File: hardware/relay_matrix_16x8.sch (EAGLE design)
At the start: 275 parts, among them J6 CT3151, J7 CT3151, J8 CT3151, U1 TM4C123GH6PMI, U2 CP2102N-A02-GQFN24R, U20 SN74HCS595, U21 SN74HCS595, U22 SN74HCS595, U23 SN74HCS595, U30 LDD-SMHTA304RISITR, U31 LDD-SMHTA304RISITR, U32 LDD-SMHTA304RISITR, U33 LDD-SMHTA304RISITR, U34 LDD-SMHTA304RISITR, U35 LDD-SMHTA304RISITR, U36 LDD-SMHTA304RISITR, U37 LDD-SMHTA304RISITR, U38 LDD-SMHTA304RISITR, U4 TLS835B2ELVSE, U5 TLS835B2ELVSE, X1 2171790001, X101 364A2595, X102 364A2595, X103 364A2595, X104 364A2595, X105 364A2595, X106 364A2595, X107 364A2595, X108 364A2595, X111 364A2595, X112 364A2595, X113 364A2595, X114 364A2595, X2 FTSH-105-01-F-DV-007-K-P, X3 SJ1-3523NG, X4 SJ1-3523NG, X5 SJ1-3523NG

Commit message: replace LDOs with more common part
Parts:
- removed U5: TLS835B2ELVSE, TLS835B2ELVSEXUMA1:TLS835B2ELVSEXUMA1
- added R33, R35: 220, rcl:R-US_R0603
- added R34: 360, rcl:R-US_R0603
- added R36: 680, rcl:R-US_R0603
- added R37, R38: 1, rcl:R-US_R0603
- added U3: NCP1117XXA, 1117:NCP1117XXA
- C10, C7: value .1uF -> 10uF; device resistor:C-USC0402 -> rcl:C-USC0805
- C11, C12: value 1uF -> 10uF; device resistor:C-USC0402 -> rcl:C-USC0805
- C8, C9: value .1uF -> 1uF
- U4: value TLS835B2ELVSE -> NCP1117XXA; device TLS835B2ELVSEXUMA1:TLS835B2ELVSEXUMA1 -> 1117:NCP1117XXA
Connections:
- net NRESET renamed !RST
- removed net 5V0: C12.1, C18.1, C31.1, C32.1, C33.1, C34.1, C35.1, C36.1, C37.1, C38.1, C39.1, C40.1, C41.1, C42.1, C43.1, C44.1, C45.1, C46.1, U100.LOADSUPPLY, U101.LOADSUPPLY, U102.LOADSUPPLY, U103.LOADSUPPLY, U104.LOADSUPPLY, U105.LOADSUPPLY, U106.LOADSUPPLY, U107.LOADSUPPLY, U108.LOADSUPPLY, U109.LOADSUPPLY, U110.LOADSUPPLY, U111.LOADSUPPLY, U112.LOADSUPPLY, U113.LOADSUPPLY, U114.LOADSUPPLY, U115.LOADSUPPLY, U5.Q, U5.SEL, U6.VCC
- removed net VDD: C1.1, C101.1, C102.1, C103.1, C104.1, C105.1, C106.1, C107.1, C108.1, C109.1, C110.1, C14.1, C15.1, C16.1, C17.1, C19.1, C2.1, C20.1, C21.1, C22.1, C23.1, C24.1, C25.1, C26.1, C27.1, C28.1, C29.1, C3.1, C30.1, C4.1, C5.1, C6.1, D1.HIGH, D2.HIGH, R14.2, R9.1, U1.VDD, U1.VDDA, U1.VDDC, U1.VDDC_2, U1.VDD_2, U1.VDD_3, U1.VDD_4, U100.LOGICSUPPLY, U101.LOGICSUPPLY, U102.LOGICSUPPLY, U103.LOGICSUPPLY, U104.LOGICSUPPLY, U105.LOGICSUPPLY, U106.LOGICSUPPLY, U107.LOGICSUPPLY, U108.LOGICSUPPLY, U109.LOGICSUPPLY, U110.LOGICSUPPLY, U111.LOGICSUPPLY, U112.LOGICSUPPLY, U113.LOGICSUPPLY, U114.LOGICSUPPLY, U115.LOGICSUPPLY, U2.VDD, U2.VIO, U2.VREGIN, U20.VCC, U21.VCC, U22.VCC, U23.VCC, X2.VCC
- new net +5V: C18.1, C31.1, C32.1, C33.1, C34.1, C35.1, C36.1, C37.1, C38.1, C39.1, C40.1, C41.1, C42.1, C43.1, C44.1, C45.1, R35.2, R38.2, U100.LOADSUPPLY, U101.LOADSUPPLY, U102.LOADSUPPLY, U103.LOADSUPPLY, U104.LOADSUPPLY, U105.LOADSUPPLY, U106.LOADSUPPLY, U107.LOADSUPPLY, U108.LOADSUPPLY, U109.LOADSUPPLY, U110.LOADSUPPLY, U111.LOADSUPPLY, U112.LOADSUPPLY, U113.LOADSUPPLY, U114.LOADSUPPLY, U115.LOADSUPPLY, U3.VOUT
- new net N$20: C9.1, R33.1, R34.2, U4.ADJ/GND
- new net N$21: C8.1, R35.1, R36.2, U3.ADJ/GND
- new net N$22: C11.1, R37.1
- new net N$23: C12.1, R38.1
- new net VDDC: C107.1, C108.1, C109.1, C110.1, U1.VDDC, U1.VDDC_2
- net +12V: now also U3.VIN, U4.VIN; no longer C8.1, C9.1, U4.EN, U4.I, U5.EN, U5.I
- net GND: now also R34.1, R36.1, S2.P$3, S2.P$4, X2.GDTCT; no longer S2.P$1, S2.P$2, U4.GND, U4.SEL, U5.GND
- net N$19: now also S2.P$1, S2.P$2; no longer S2.P$3, S2.P$4
- net VBUS: now also C46.1, U6.VCC; no longer U6.IO3
- net VCC: now also C1.1, C101.1, C102.1, C103.1, C104.1, C105.1, C106.1, C14.1, C15.1, C16.1, C17.1, C19.1, C2.1, C20.1, C21.1, C22.1, C23.1, C24.1, C25.1, C26.1, C27.1, C28.1, C29.1, C3.1, C30.1, C4.1, C5.1, C6.1, D1.HIGH, D2.HIGH, R14.2, R33.2, R37.2, R9.1, U1.VDD, U1.VDDA, U1.VDD_2, U1.VDD_3, U1.VDD_4, U100.LOGICSUPPLY, U101.LOGICSUPPLY, U102.LOGICSUPPLY, U103.LOGICSUPPLY, U104.LOGICSUPPLY, U105.LOGICSUPPLY, U106.LOGICSUPPLY, U107.LOGICSUPPLY, U108.LOGICSUPPLY, U109.LOGICSUPPLY, U110.LOGICSUPPLY, U111.LOGICSUPPLY, U112.LOGICSUPPLY, U113.LOGICSUPPLY, U114.LOGICSUPPLY, U115.LOGICSUPPLY, U2.VDD, U2.VIO, U2.VREGIN, U20.VCC, U21.VCC, U22.VCC, U23.VCC, U4.VOUT, X2.VCC; no longer C11.1, U4.Q
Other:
- note added: "Microcontroller"
- note added: "Power connectors"
- note added: "UART connectors"
- note added: "Voltage regulators"

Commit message: version sent to pcbway
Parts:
- added C47: 100n, resistor:C-USC0402
- added U5: ECS-2033-080-AU, ecs-20xx:ECS-2033-080-AU
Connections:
- new net OSC: U1.XOSC0, U5.OSC
- net GND: now also C47.2, U5.GND
- net VCC: now also C47.1, U5.EN, U5.VDD
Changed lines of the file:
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@@
 <part name="R37" library="rcl" library_urn="urn:adsk.eagle:library:334" deviceset="R-US_" device="R0603" package3d_urn="urn:adsk.eagle:package:23555/3" value="1"/>
 <part name="R38" library="rcl" library_urn="urn:adsk.eagle:library:334" deviceset="R-US_" device="R0603" package3d_urn="urn:adsk.eagle:package:23555/3" value="1"/>
+<part name="U5" library="ecs-20xx" deviceset="ECS-2033-080-AU" device="" package3d_urn="urn:adsk.eagle:package:34367365/1"/>
+<part name="P+2" library="supply1" library_urn="urn:adsk.eagle:library:371" deviceset="VCC" device=""/>
+<part name="GND2" library="supply1" library_urn="urn:adsk.eagle:library:371" deviceset="GND" device=""/>
+<part name="C47" library="resistor" library_urn="urn:adsk.eagle:library:348" deviceset="C-US" device="C0402" package3d_urn="urn:adsk.eagle:package:23626/2" value="100n"/>
+<part name="GND28" library="supply1" library_urn="urn:adsk.eagle:library:371" deviceset="GND" device=""/>
 </parts>
 <sheets>
@@
 <instance part="GND22" gate="1" x="20.32" y="-20.32" smashed="yes">
 <attribute name="VALUE" x="17.78" y="-22.86" size="1.778" layer="96"/>
+</instance>
+<instance part="U5" gate="G$1" x="144.78" y="-53.34" smashed="yes"/>
+<instance part="P+2" gate="VCC" x="137.16" y="-50.8" smashed="yes">
+<attribute name="VALUE" x="134.62" y="-53.34" size="1.778" layer="96" rot="R90"/>
+</instance>
+<instance part="GND2" gate="1" x="137.16" y="-78.74" smashed="yes">
+<attribute name="VALUE" x="134.62" y="-81.28" size="1.778" layer="96"/>
+</instance>
+<instance part="C47" gate="G$1" x="132.08" y="-63.5" smashed="yes">
+<attribute name="NAME" x="133.096" y="-62.865" size="1.778" layer="95"/>
+<attribute name="VALUE" x="133.096" y="-67.691" size="1.778" layer="96"/>
+</instance>
+<instance part="GND28" gate="1" x="132.08" y="-72.39" smashed="yes">
+<attribute name="VALUE" x="129.54" y="-74.93" size="1.778" layer="96"/>
 </instance>
 </instances>
@@
 <pinref part="GND12" gate="1" pin="GND"/>
 </segment>
+<segment>
+<pinref part="GND2" gate="1" pin="GND"/>
+<wire x1="137.16" y1="-76.2" x2="137.16" y2="-73.66" width="0.1524" layer="91"/>
+<pinref part="U5" gate="G$1" pin="GND"/>
+<wire x1="137.16" y1="-73.66" x2="139.7" y2="-73.66" width="0.1524" layer="91"/>
+</segment>
+<segment>
+<pinref part="C47" gate="G$1" pin="2"/>
+<pinref part="GND28" gate="1" pin="GND"/>
+<wire x1="132.08" y1="-69.85" x2="132.08" y2="-68.58" width="0.1524" layer="91"/>
+</segment>
 </net>
 <net name="MCU_RX_PAR" class="0">
@@
 <pinref part="P+14" gate="VCC" pin="VCC"/>
 </segment>
+<segment>
+<pinref part="P+2" gate="VCC" pin="VCC"/>
+<wire x1="137.16" y1="-53.34" x2="137.16" y2="-55.88" width="0.1524" layer="91"/>
+<pinref part="U5" gate="G$1" pin="EN"/>
+<wire x1="137.16" y1="-55.88" x2="137.16" y2="-58.42" width="0.1524" layer="91"/>
+<wire x1="137.16" y1="-58.42" x2="137.16" y2="-60.96" width="0.1524" layer="91"/>
+<wire x1="137.16" y1="-60.96" x2="139.7" y2="-60.96" width="0.1524" layer="91"/>
+<pinref part="U5" gate="G$1" pin="VDD"/>
+<wire x1="139.7" y1="-55.88" x2="137.16" y2="-55.88" width="0.1524" layer="91"/>
+<junction x="137.16" y="-55.88"/>
+<wire x1="137.16" y1="-58.42" x2="132.08" y2="-58.42" width="0.1524" layer="91"/>
+<wire x1="132.08" y1="-58.42" x2="132.08" y2="-60.96" width="0.1524" layer="91"/>
+<pinref part="C47" gate="G$1" pin="1"/>
+<junction x="137.16" y="-58.42"/>
+</segment>
 </net>
 <net name="!RST" class="0">
@@
 </segment>
 </net>
+<net name="OSC" class="0">
+<segment>
+<pinref part="U5" gate="G$1" pin="OSC"/>
+<wire x1="167.64" y1="-55.88" x2="172.72" y2="-55.88" width="0.1524" layer="91"/>
+<label x="172.72" y="-55.88" size="1.27" layer="95" xref="yes"/>
+</segment>
+<segment>
+<pinref part="U1" gate="A" pin="XOSC0"/>
+<wire x1="91.44" y1="16.51" x2="96.52" y2="16.51" width="0.1524" layer="91"/>
+<label x="96.52" y="16.51" size="1.27" layer="95" xref="yes"/>
+</segment>
+</net>

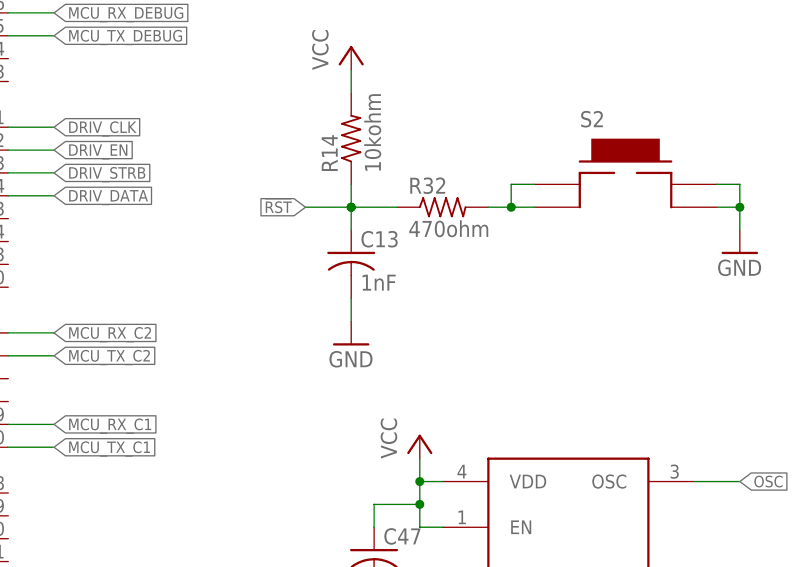
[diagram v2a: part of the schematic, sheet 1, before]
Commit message: finish filling out part ordering info
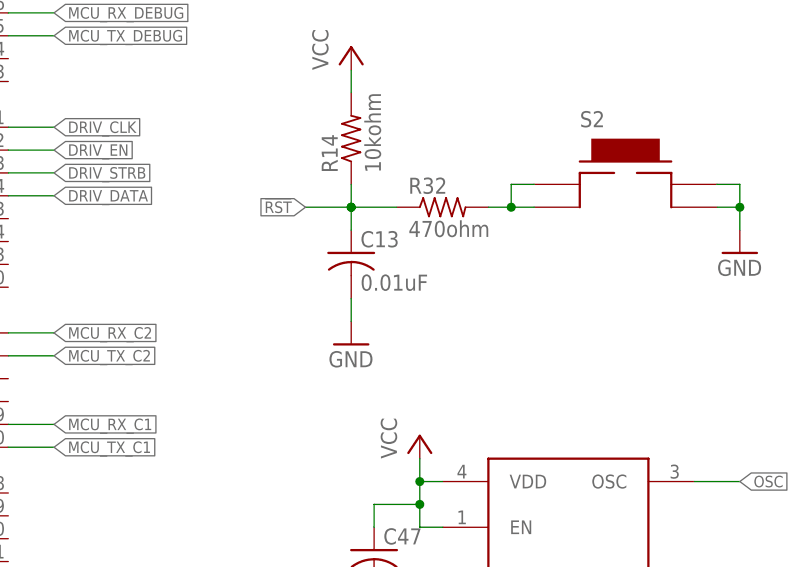
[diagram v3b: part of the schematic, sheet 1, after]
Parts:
- C1, C101, C102, C106, C107, C109, C2, C3, C4, C46, C47: MANUFACTURER_PART_NUMBER (none) -> CL05B104KO5NNNC; MFR_NAME (none) -> Samsung Electro-Mechanics
- C10, C11, C12, C7: MANUFACTURER_PART_NUMBER (none) -> CL21A106KAYNNNE; MFR_NAME (none) -> Samsung Electro-Mechanics
- C103, C104: MANUFACTURER_PART_NUMBER (none) -> GCM155R71H103KA55D; MFR_NAME (none) -> Murata Electronics
- C105, C110, C14, C15, C16, C17, C18, C19, C20, C21, C22, C23, C24, C25, C26, C27, C28, C29, C30, C31, C32, C33, C34, C35, C36, C37, C38, C39, C40, C41, C42, C43, C44, C45, C6, C8, C9: MANUFACTURER_PART_NUMBER (none) -> CL05A105KO5NNNC; MFR_NAME (none) -> Samsung Electro-Mechanics
- C108: MANUFACTURER_PART_NUMBER (none) -> CL10A225KO8NNNC; MFR_NAME (none) -> Samsung Electro-Mechanics
- C13: value 1nF -> 0.01uF; MANUFACTURER_PART_NUMBER (none) -> GCM155R71H103KA55D; MFR_NAME (none) -> Murata Electronics
- C5: MANUFACTURER_PART_NUMBER (none) -> CL10A475KA8NQNC; MFR_NAME (none) -> Samsung Electro-Mechanics
- R10, R11: MANUFACTURER_PART_NUMBER (none) -> RC0402FR-075K1L; MFR_NAME (none) -> YAGEO
- R12: MANUFACTURER_PART_NUMBER (none) -> RMCF0402FT47K5; MFR_NAME (none) -> Stackpole Electronics Inc
- R13: MANUFACTURER_PART_NUMBER (none) -> RC0402FR-0722K1L; MFR_NAME (none) -> YAGEO
- R14: MANUFACTURER_PART_NUMBER (none) -> RC1005F103CS; MFR_NAME (none) -> Samsung Electro-Mechanics
- R32: MANUFACTURER_PART_NUMBER (none) -> RC0402JR-07470RL; MFR_NAME (none) -> YAGEO
- R33, R35: MANUFACTURER_PART_NUMBER (none) -> RC1608F221CS; MFR_NAME (none) -> Samsung Electro-Mechanics
- R34: MANUFACTURER_NAME (none) -> YAGEO; MANUFACTURER_PART_NUMBER (none) -> RC0603FR-07360RL
- R36: MANUFACTURER_PART_NUMBER (none) -> RC0603FR-07680RL; MFR_NAME (none) -> YAGEO
- R9: MANUFACTURER_PART_NUMBER (none) -> CRG0402F1K0; MFR_NAME (none) -> TE Connectivity Passive Product
- S2: MANUFACTURER_PART_NUMBER (none) -> FSM4JSMA; MFR_NAME (none) -> TE Connectivity
- U20, U21, U22, U23: MANUFACTURER_PART_NUMBER (none) -> SN74HCS595PWR; MFR_NAME (none) -> Texas Instruments
- U3, U4: MANUFACTURER_PART_NUMBER (none) -> NCP1117IDTAT4G; MFR_NAME (none) -> ON Semiconductor
- U30, U31, U32, U33, U34, U35, U36, U37, U38: MANUFACTURER_PART_NUMBER (none) -> LDD-SMHTA304RISITR; MFR_NAME (none) -> Lumex Opto/Components Inc.
- U5: MANUFACTURER_PART_NUMBER (none) -> ECS-2033-080-AU; MFR_NAME (none) -> ECS Incorporated
- X101, X102, X103, X104, X105, X106, X107, X108, X111, X112, X113, X114: MANUFACTURER_PART_NUMBER (none) -> 364A2595; MFR_NAME (none) -> Winchester Interconnect
- X2: MANUFACTURER_PART_NUMBER (none) -> FTSH-105-01-F-DV-007-K-P; MFR_NAME (none) -> Samtec
- X3, X4, X5: MANUFACTURER_PART_NUMBER (none) -> SJ1-3523NG; MFR_NAME (none) -> CUI Devices

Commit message: add more part names
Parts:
- K0, K1, K10, K100, K101, K102, K103, K104, K105, K106, K107, K108, K109, K11, K110, K111, K112, K113, K114, K115, K116, K117, K118, K119, K12, K120, K121, K122, K123, K124, K125, K126, K127, K13, K14, K15, K16, K17, K18, K19, K2, K20, K21, K22, K23, K24, K25, K26, K27, K28, K29, K3, K30, K31, K32, K33, K34, K35, K36, K37, K38, K39, K4, K40, K41, K42, K43, K44, K45, K46, K47, K48, K49, K5, K50, K51, K52, K53, K54, K55, K56, K57, K58, K59, K6, K60, K61, K62, K63, K64, K65, K66, K67, K68, K69, K7, K70, K71, K72, K73, K74, K75, K76, K77, K78, K79, K8, K80, K81, K82, K83, K84, K85, K86, K87, K88, K89, K9, K90, K91, K92, K93, K94, K95, K96, K97, K98, K99: MANUFACTURER_PART_NUMBER (none) -> G6L-1F-DC4.5; MFR_NAME (none) -> Omron Electronics Inc-EMC Div
- R34: MANUFACTURER_NAME YAGEO -> (none); MFR_NAME (none) -> YAGEO
- R37, R38: MANUFACTURER_PART_NUMBER (none) -> RC0603FR-071RL; MFR_NAME (none) -> YAGEO
